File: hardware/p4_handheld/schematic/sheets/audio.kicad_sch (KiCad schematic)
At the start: 0 parts

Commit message: hw(p4_handheld): audio, storage, debug sheets
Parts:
- added C4: 10u, C0603, symbol Device:C
- added J5: Speaker-2pin, TBD, symbol PSP4H:Block2
- added U7: MAX98357A, TQFN-16-EP-3x3-TBD, symbol PSP4H:Block2
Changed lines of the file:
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@@
     (comment 2 "Same-net labels connect; globals cross sheets")
   )
+  (symbol (lib_id "PSP4H:Block2") (at 35 35 0) (unit 1)
+    (exclude_from_sim no) (in_bom yes) (on_board yes) (dnp no) (fields_autoplaced)
+    (property "Reference" "U7" (at 35 29 0)
+      (effects (font (size 1.27 1.27))))
+    (property "Value" "MAX98357A" (at 35 41 0)
+      (effects (font (size 1.27 1.27))))
+    (property "Footprint" "TQFN-16-EP-3x3-TBD" (at 35 35 0)
+      (effects (font (size 1.27 1.27)) hide))
+    (property "Datasheet" "~" (at 35 35 0)
+      (effects (font (size 1.27 1.27)) hide))
+    (instances (project "card" (path "/p4_handheld/sheets/audio" (reference "U7") (unit 1))))
+  )
+  (label "+3V3" (at 53 40 0) (fields_autoplaced)
+    (effects (font (size 1.27 1.27)) (justify left)))
+  (label "GND" (at 53 40 0) (fields_autoplaced)
+    (effects (font (size 1.27 1.27)) (justify left)))
+  (label "I2S_BCLK" (at 53 30 0) (fields_autoplaced)
+    (effects (font (size 1.27 1.27)) (justify left)))
+  (label "I2S_LRCLK" (at 53 40 0) (fields_autoplaced)
+    (effects (font (size 1.27 1.27)) (justify left)))
+  (label "I2S_DIN" (at 53 32.5 0) (fields_autoplaced)
+    (effects (font (size 1.27 1.27)) (justify left)))
+  (label "AMP_SD_MODE" (at 53 30 0) (fields_autoplaced)
+    (effects (font (size 1.27 1.27)) (justify left)))
+  (label "SPK+" (at 53 37.5 0) (fields_autoplaced)
+    (effects (font (size 1.27 1.27)) (justify left)))
+  (label "SPK-" (at 53 37.5 0) (fields_autoplaced)
+    (effects (font (size 1.27 1.27)) (justify left)))
+  (symbol (lib_id "PSP4H:Block2") (at 80 35 0) (unit 1)
+    (exclude_from_sim no) (in_bom yes) (on_board yes) (dnp no) (fields_autoplaced)
+    (property "Reference" "J5" (at 80 29 0)
+      (effects (font (size 1.27 1.27))))
+    (property "Value" "Speaker-2pin" (at 80 41 0)
+      (effects (font (size 1.27 1.27))))
+    (property "Footprint" "TBD" (at 80 35 0)
+      (effects (font (size 1.27 1.27)) hide))
+    (property "Datasheet" "~" (at 80 35 0)
+      (effects (font (size 1.27 1.27)) hide))
+    (property "Gate" "GATE-SPEAKER-SELECT" (at 80 35 0)
+      (effects (font (size 1.27 1.27)) hide))
+    (instances (project "card" (path "/p4_handheld/sheets/audio" (reference "J5") (unit 1))))
+  )
+  (label "SPK+" (at 98 30 0) (fields_autoplaced)
+    (effects (font (size 1.27 1.27)) (justify left)))
+  (label "SPK-" (at 98 32.5 0) (fields_autoplaced)
+    (effects (font (size 1.27 1.27)) (justify left)))
+  (symbol (lib_id "Device:C") (at 125 35 0) (unit 1)
+    (exclude_from_sim no) (in_bom yes) (on_board yes) (dnp no) (fields_autoplaced)
+    (property "Reference" "C4" (at 125 29 0)
+      (effects (font (size 1.27 1.27))))
+    (property "Value" "10u" (at 125 41 0)
+      (effects (font (size 1.27 1.27))))
+    (property "Footprint" "C0603" (at 125 35 0)
+      (effects (font (size 1.27 1.27)) hide))
+    (property "Datasheet" "~" (at 125 35 0)
+      (effects (font (size 1.27 1.27)) hide))
+    (property "LCSC" "C19702" (at 125 35 0)
+      (effects (font (size 1.27 1.27)) hide))
+    (property "MPN" "CL10A106KP8NNNC" (at 125 35 0)
+      (effects (font (size 1.27 1.27)) hide))
+    (instances (project "card" (path "/p4_handheld/sheets/audio" (reference "C4") (unit 1))))
+  )
+  (label "+3V3" (at 143 30 0) (fields_autoplaced)
+    (effects (font (size 1.27 1.27)) (justify left)))
+  (label "GND" (at 143 32.5 0) (fields_autoplaced)
+    (effects (font (size 1.27 1.27)) (justify left)))
+  (global_label "+3V3" (shape input) (at 280 20 0) (fields_autoplaced)
+    (effects (font (size 1.27 1.27)) (justify left))
+    (property "Intersheetrefs" "${INTERSHEET_REFS}" (at 280 20 0)
+      (effects (font (size 1.27 1.27)) hide))
+  )
+  (global_label "GND" (shape input) (at 280 26 0) (fields_autoplaced)
+    (effects (font (size 1.27 1.27)) (justify left))
+    (property "Intersheetrefs" "${INTERSHEET_REFS}" (at 280 26 0)
+      (effects (font (size 1.27 1.27)) hide))
+  )
+  (global_label "I2S_BCLK" (shape input) (at 280 32 0) (fields_autoplaced)
+    (effects (font (size 1.27 1.27)) (justify left))
+    (property "Intersheetrefs" "${INTERSHEET_REFS}" (at 280 32 0)
+      (effects (font (size 1.27 1.27)) hide))
+  )
+  (global_label "I2S_LRCLK" (shape input) (at 280 38 0) (fields_autoplaced)
+    (effects (font (size 1.27 1.27)) (justify left))
+    (property "Intersheetrefs" "${INTERSHEET_REFS}" (at 280 38 0)
+      (effects (font (size 1.27 1.27)) hide))
+  )
+  (global_label "I2S_DIN" (shape input) (at 280 44 0) (fields_autoplaced)
+    (effects (font (size 1.27 1.27)) (justify left))
+    (property "Intersheetrefs" "${INTERSHEET_REFS}" (at 280 44 0)
+      (effects (font (size 1.27 1.27)) hide))
+  )
+  (global_label "AMP_SD_MODE" (shape input) (at 280 50 0) (fields_autoplaced)
+    (effects (font (size 1.27 1.27)) (justify left))
+    (property "Intersheetrefs" "${INTERSHEET_REFS}" (at 280 50 0)
+      (effects (font (size 1.27 1.27)) hide))
+  )
 )

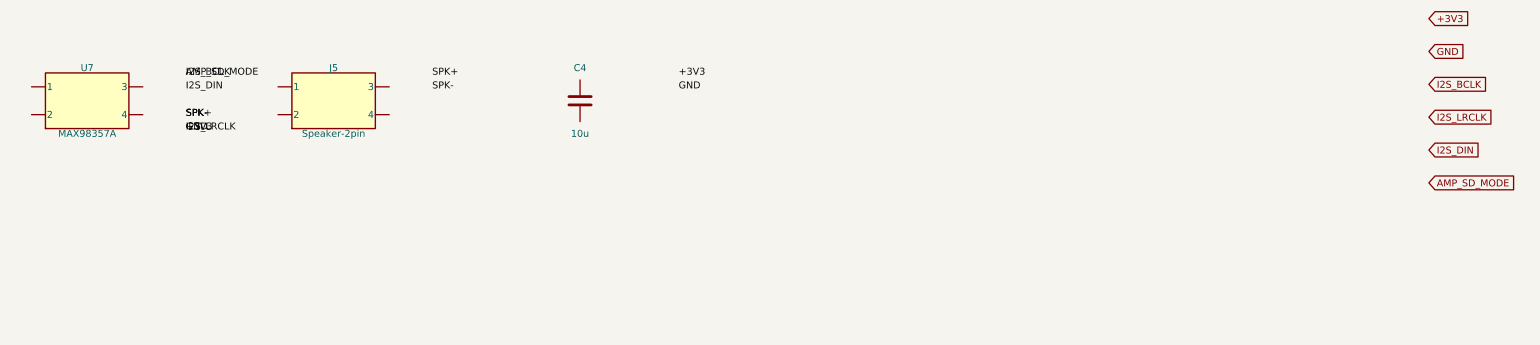
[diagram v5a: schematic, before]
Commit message: hw(p4_handheld): ERC-clean schematic engine (real pins, on-endpoint labels, project symbol lib)
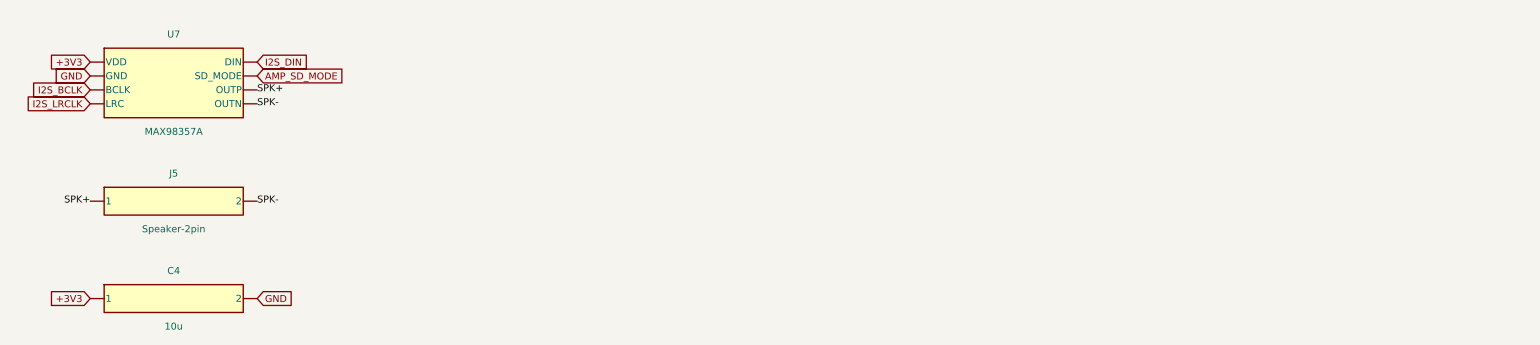
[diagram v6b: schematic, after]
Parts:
- removed C4: 10u, C0603, symbol Device:C
- removed J5: Speaker-2pin, TBD, symbol PSP4H:Block2
- removed U7: MAX98357A, TQFN-16-EP-3x3-TBD, symbol PSP4H:Block2
- added C4: 10u, symbol PSP4H:SYM_C4
- added J5: Speaker-2pin, symbol PSP4H:SYM_J5
- added U7: MAX98357A, symbol PSP4H:SYM_U7
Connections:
- net +3V3: now also C4.1, U7.VDD
- net AMP_SD_MODE: now also U7.SD_MODE
- net I2S_DIN: now also U7.DIN
- net SPK+: now also J5.1, U7.OUTP
- new net GND: C4.2, U7.GND
- new net I2S_BCLK: U7.BCLK
- new net I2S_LRCLK: U7.LRC
- new net SPK-: J5.2, U7.OUTN
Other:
- title: PuzzleScript Card — audio -> PuzzleScript P4 Handheld — audio
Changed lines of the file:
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@@
   (generator "PuzzleScript generate_kicad.js")
   (generator_version "1.0")
-  (paper "A4")
+  (paper "A3")
   (title_block
-    (title "PuzzleScript Card — audio")
+    (title "PuzzleScript P4 Handheld — audio")
     (date "2026-07-12")
-    (rev "spin1")
+    (rev "circuit-phase-0")
     (comment 1 "Auto-generated from connectivity.json")
-    (comment 2 "Same-net labels connect; globals cross sheets")
+    (comment 2 "Labels sit on pin endpoints; globals cross sheets")
   )
-  (symbol (lib_id "PSP4H:Block2") (at 35 35 0) (unit 1)
-    (exclude_from_sim no) (in_bom yes) (on_board yes) (dnp no) (fields_autoplaced)
-    (property "Reference" "U7" (at 35 29 0)
+  (symbol (lib_id "PSP4H:SYM_U7") (at 50.8 31.75 0) (unit 1)
+    (exclude_from_sim no) (in_bom yes) (on_board yes) (dnp no)
+    (property "Reference" "U7" (at 50.8 22.86 0)
       (effects (font (size 1.27 1.27))))
-    (property "Value" "MAX98357A" (at 35 41 0)
+    (property "Value" "MAX98357A" (at 50.8 40.64 0)
       (effects (font (size 1.27 1.27))))
-    (property "Footprint" "TQFN-16-EP-3x3-TBD" (at 35 35 0)
+    (property "Footprint" "" (at 50.8 31.75 0)
       (effects (font (size 1.27 1.27)) hide))
-    (property "Datasheet" "~" (at 35 35 0)
+    (property "FootprintPlan" "TQFN-16-EP-3x3-TBD" (at 50.8 31.75 0)
       (effects (font (size 1.27 1.27)) hide))
-    (instances (project "card" (path "/p4_handheld/sheets/audio" (reference "U7") (unit 1))))
+    (property "Datasheet" "~" (at 50.8 31.75 0)
+      (effects (font (size 1.27 1.27)) hide))
+    (pin "VDD")
+    (pin "GND")
+    (pin "BCLK")
+    (pin "LRC")
+    (pin "DIN")
+    (pin "SD_MODE")
+    (pin "OUTP")
+    (pin "OUTN")
+    (instances (project "p4_handheld" (path "/p4_handheld/sheets/audio" (reference "U7") (unit 1))))
   )
-  (label "+3V3" (at 53 40 0) (fields_autoplaced)
-    (effects (font (size 1.27 1.27)) (justify left)))
-  (label "GND" (at 53 40 0) (fields_autoplaced)
-    (effects (font (size 1.27 1.27)) (justify left)))
-  (label "I2S_BCLK" (at 53 30 0) (fields_autoplaced)
-    (effects (font (size 1.27 1.27)) (justify left)))
-  (label "I2S_LRCLK" (at 53 40 0) (fields_autoplaced)
-    (effects (font (size 1.27 1.27)) (justify left)))
-  (label "I2S_DIN" (at 53 32.5 0) (fields_autoplaced)
-    (effects (font (size 1.27 1.27)) (justify left)))
-  (label "AMP_SD_MODE" (at 53 30 0) (fields_autoplaced)
-    (effects (font (size 1.27 1.27)) (justify left)))
-  (label "SPK+" (at 53 37.5 0) (fields_autoplaced)
-    (effects (font (size 1.27 1.27)) (justify left)))
-  (label "SPK-" (at 53 37.5 0) (fields_autoplaced)
-    (effects (font (size 1.27 1.27)) (justify left)))
-  (symbol (lib_id "PSP4H:Block2") (at 80 35 0) (unit 1)
-    (exclude_from_sim no) (in_bom yes) (on_board yes) (dnp no) (fields_autoplaced)
-    (property "Reference" "J5" (at 80 29 0)
-      (effects (font (size 1.27 1.27))))
-    (property "Value" "Speaker-2pin" (at 80 41 0)
-      (effects (font (size 1.27 1.27))))
-    (property "Footprint" "TBD" (at 80 35 0)
-      (effects (font (size 1.27 1.27)) hide))
-    (property "Datasheet" "~" (at 80 35 0)
-      (effects (font (size 1.27 1.27)) hide))
-    (property "Gate" "GATE-SPEAKER-SELECT" (at 80 35 0)
-      (effects (font (size 1.27 1.27)) hide))
-    (instances (project "card" (path "/p4_handheld/sheets/audio" (reference "J5") (unit 1))))
-  )
-  (label "SPK+" (at 98 30 0) (fields_autoplaced)
-    (effects (font (size 1.27 1.27)) (justify left)))
-  (label "SPK-" (at 98 32.5 0) (fields_autoplaced)
-    (effects (font (size 1.27 1.27)) (justify left)))
-  (symbol (lib_id "Device:C") (at 125 35 0) (unit 1)
-    (exclude_from_sim no) (in_bom yes) (on_board yes) (dnp no) (fields_autoplaced)
-    (property "Reference" "C4" (at 125 29 0)
-      (effects (font (size 1.27 1.27))))
-    (property "Value" "10u" (at 125 41 0)
-      (effects (font (size 1.27 1.27))))
-    (property "Footprint" "C0603" (at 125 35 0)
-      (effects (font (size 1.27 1.27)) hide))
-    (property "Datasheet" "~" (at 125 35 0)
-      (effects (font (size 1.27 1.27)) hide))
-    (property "LCSC" "C19702" (at 125 35 0)
-      (effects (font (size 1.27 1.27)) hide))
-    (property "MPN" "CL10A106KP8NNNC" (at 125 35 0)
-      (effects (font (size 1.27 1.27)) hide))
-    (instances (project "card" (path "/p4_handheld/sheets/audio" (reference "C4") (unit 1))))
-  )
-  (label "+3V3" (at 143 30 0) (fields_autoplaced)
-    (effects (font (size 1.27 1.27)) (justify left)))
-  (label "GND" (at 143 32.5 0) (fields_autoplaced)
-    (effects (font (size 1.27 1.27)) (justify left)))
-  (global_label "+3V3" (shape input) (at 280 20 0) (fields_autoplaced)
-    (effects (font (size 1.27 1.27)) (justify left))
-    (property "Intersheetrefs" "${INTERSHEET_REFS}" (at 280 20 0)
+  (global_label "+3V3" (shape input) (at 35.56 27.94 180) (fields_autoplaced)
+    (effects (font (size 1.27 1.27)) (justify right))
+    (property "Intersheetrefs" "${INTERSHEET_REFS}" (at 35.56 27.94 0)
       (effects (font (size 1.27 1.27)) hide))
   )
-  (global_label "GND" (shape input) (at 280 26 0) (fields_autoplaced)
-    (effects (font (size 1.27 1.27)) (justify left))
-    (property "Intersheetrefs" "${INTERSHEET_REFS}" (at 280 26 0)
+  (global_label "GND" (shape input) (at 35.56 30.48 180) (fields_autoplaced)
+    (effects (font (size 1.27 1.27)) (justify right))
+    (property "Intersheetrefs" "${INTERSHEET_REFS}" (at 35.56 30.48 0)
       (effects (font (size 1.27 1.27)) hide))
   )
-  (global_label "I2S_BCLK" (shape input) (at 280 32 0) (fields_autoplaced)
-    (effects (font (size 1.27 1.27)) (justify left))
-    (property "Intersheetrefs" "${INTERSHEET_REFS}" (at 280 32 0)
+  (global_label "I2S_BCLK" (shape input) (at 35.56 33.02 180) (fields_autoplaced)
+    (effects (font (size 1.27 1.27)) (justify right))
+    (property "Intersheetrefs" "${INTERSHEET_REFS}" (at 35.56 33.02 0)
       (effects (font (size 1.27 1.27)) hide))
   )
-  (global_label "I2S_LRCLK" (shape input) (at 280 38 0) (fields_autoplaced)
-    (effects (font (size 1.27 1.27)) (justify left))
-    (property "Intersheetrefs" "${INTERSHEET_REFS}" (at 280 38 0)
+  (global_label "I2S_LRCLK" (shape input) (at 35.56 35.56 180) (fields_autoplaced)
+    (effects (font (size 1.27 1.27)) (justify right))
+    (property "Intersheetrefs" "${INTERSHEET_REFS}" (at 35.56 35.56 0)
       (effects (font (size 1.27 1.27)) hide))
   )
-  (global_label "I2S_DIN" (shape input) (at 280 44 0) (fields_autoplaced)
+  (global_label "I2S_DIN" (shape input) (at 66.04 27.94 0) (fields_autoplaced)
     (effects (font (size 1.27 1.27)) (justify left))
-    (property "Intersheetrefs" "${INTERSHEET_REFS}" (at 280 44 0)
+    (property "Intersheetrefs" "${INTERSHEET_REFS}" (at 66.04 27.94 0)
       (effects (font (size 1.27 1.27)) hide))
   )
-  (global_label "AMP_SD_MODE" (shape input) (at 280 50 0) (fields_autoplaced)
+  (global_label "AMP_SD_MODE" (shape input) (at 66.04 30.48 0) (fields_autoplaced)
     (effects (font (size 1.27 1.27)) (justify left))
-    (property "Intersheetrefs" "${INTERSHEET_REFS}" (at 280 50 0)
+    (property "Intersheetrefs" "${INTERSHEET_REFS}" (at 66.04 30.48 0)
       (effects (font (size 1.27 1.27)) hide))
   )
+  (label "SPK+" (at 66.04 33.02 0) (fields_autoplaced)
+    (effects (font (size 1.27 1.27)) (justify left)))
+  (label "SPK-" (at 66.04 35.56 0) (fields_autoplaced)
+    (effects (font (size 1.27 1.27)) (justify left)))
+  (symbol (lib_id "PSP4H:SYM_J5") (at 50.8 53.34 0) (unit 1)
+    (exclude_from_sim no) (in_bom yes) (on_board yes) (dnp no)
+    (property "Reference" "J5" (at 50.8 48.26 0)
+      (effects (font (size 1.27 1.27))))
+    (property "Value" "Speaker-2pin" (at 50.8 58.42 0)
+      (effects (font (size 1.27 1.27))))
+    (property "Footprint" "" (at 50.8 53.34 0)
+      (effects (font (size 1.27 1.27)) hide))
+    (property "FootprintPlan" "TBD" (at 50.8 53.34 0)
+      (effects (font (size 1.27 1.27)) hide))
+    (property "Datasheet" "~" (at 50.8 53.34 0)
+      (effects (font (size 1.27 1.27)) hide))
+    (property "Gate" "GATE-SPEAKER-SELECT" (at 50.8 53.34 0)
+      (effects (font (size 1.27 1.27)) hide))
+    (pin "1")
+    (pin "2")
+    (instances (project "p4_handheld" (path "/p4_handheld/sheets/audio" (reference "J5") (unit 1))))
+  )
+  (label "SPK+" (at 35.56 53.34 180) (fields_autoplaced)
+    (effects (font (size 1.27 1.27)) (justify right)))
+  (label "SPK-" (at 66.04 53.34 0) (fields_autoplaced)
+    (effects (font (size 1.27 1.27)) (justify left)))
+  (symbol (lib_id "PSP4H:SYM_C4") (at 50.8 71.12 0) (unit 1)
+    (exclude_from_sim no) (in_bom yes) (on_board yes) (dnp no)
+    (property "Reference" "C4" (at 50.8 66.04 0)
+      (effects (font (size 1.27 1.27))))
+    (property "Value" "10u" (at 50.8 76.2 0)
+      (effects (font (size 1.27 1.27))))
+    (property "Footprint" "" (at 50.8 71.12 0)
+      (effects (font (size 1.27 1.27)) hide))
+    (property "FootprintPlan" "C0603" (at 50.8 71.12 0)
+      (effects (font (size 1.27 1.27)) hide))
+    (property "Datasheet" "~" (at 50.8 71.12 0)
+      (effects (font (size 1.27 1.27)) hide))
+    (property "LCSC" "C19702" (at 50.8 71.12 0)
+      (effects (font (size 1.27 1.27)) hide))
+    (property "MPN" "CL10A106KP8NNNC" (at 50.8 71.12 0)
+      (effects (font (size 1.27 1.27)) hide))
+    (pin "1")
+    (pin "2")
+    (instances (project "p4_handheld" (path "/p4_handheld/sheets/audio" (reference "C4") (unit 1))))
+  )
+  (global_label "+3V3" (shape input) (at 35.56 71.12 180) (fields_autoplaced)
+    (effects (font (size 1.27 1.27)) (justify right))
+    (property "Intersheetrefs" "${INTERSHEET_REFS}" (at 35.56 71.12 0)
+      (effects (font (size 1.27 1.27)) hide))
+  )
+  (global_label "GND" (shape input) (at 66.04 71.12 0) (fields_autoplaced)
+    (effects (font (size 1.27 1.27)) (justify left))
+    (property "Intersheetrefs" "${INTERSHEET_REFS}" (at 66.04 71.12 0)
+      (effects (font (size 1.27 1.27)) hide))
+  )

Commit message: hw(p4_handheld): JLC-checked BOM and availability record
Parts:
- J5: FootprintPlan TBD -> CONN-SMD_SM02B-SRSS-TB; LCSC (none) -> C160404; MPN (none) -> SM02B-SRSS-TB(LF)(SN)
- U7: FootprintPlan TQFN-16-EP-3x3-TBD -> TQFN-16_L3.0-W3.0-P0.50-EP; LCSC (none) -> C910544; MPN (none) -> MAX98357AETE+T
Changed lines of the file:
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@@
     (property "Footprint" "" (at 50.8 31.75 0)
       (effects (font (size 1.27 1.27)) hide))
-    (property "FootprintPlan" "TQFN-16-EP-3x3-TBD" (at 50.8 31.75 0)
+    (property "FootprintPlan" "TQFN-16_L3.0-W3.0-P0.50-EP" (at 50.8 31.75 0)
       (effects (font (size 1.27 1.27)) hide))
     (property "Datasheet" "~" (at 50.8 31.75 0)
+      (effects (font (size 1.27 1.27)) hide))
+    (property "LCSC" "C910544" (at 50.8 31.75 0)
+      (effects (font (size 1.27 1.27)) hide))
+    (property "MPN" "MAX98357AETE+T" (at 50.8 31.75 0)
       (effects (font (size 1.27 1.27)) hide))
     (pin "VDD")
@@
     (property "Footprint" "" (at 50.8 53.34 0)
       (effects (font (size 1.27 1.27)) hide))
-    (property "FootprintPlan" "TBD" (at 50.8 53.34 0)
+    (property "FootprintPlan" "CONN-SMD_SM02B-SRSS-TB" (at 50.8 53.34 0)
       (effects (font (size 1.27 1.27)) hide))
     (property "Datasheet" "~" (at 50.8 53.34 0)
@@
     (property "Gate" "GATE-SPEAKER-SELECT" (at 50.8 53.34 0)
       (effects (font (size 1.27 1.27)) hide))
+    (property "LCSC" "C160404" (at 50.8 53.34 0)
+      (effects (font (size 1.27 1.27)) hide))
+    (property "MPN" "SM02B-SRSS-TB(LF)(SN)" (at 50.8 53.34 0)
+      (effects (font (size 1.27 1.27)) hide))
     (pin "1")
